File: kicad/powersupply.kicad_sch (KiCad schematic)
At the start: 41 parts, among them Q1 BC547, Q2 BC557, Q3 AO3401A, Q4 AO3401A, SW1 SW_Push, U1 MCP602, U2 INA219AxDCN, U3 STM32F103CBTx, U4 CR2013-MI2120, U5 MCP602, U6 MCP602, U7 MCP602, U8 PCF8574, U9 MCP4725

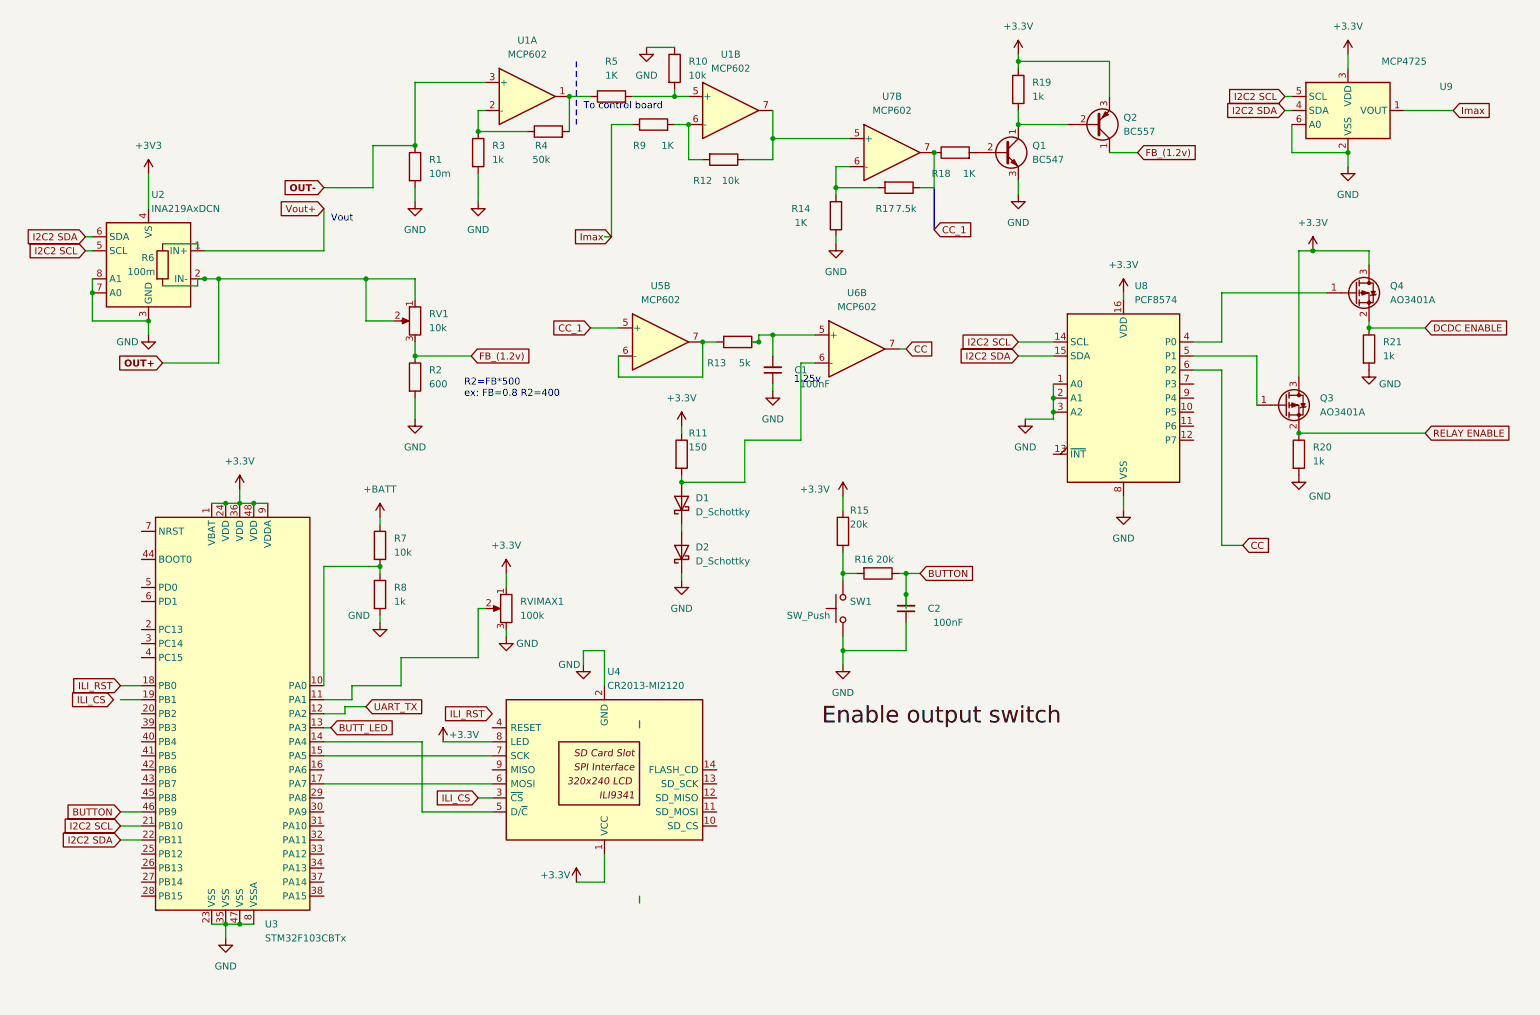
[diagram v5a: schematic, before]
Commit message: update kicad schematic with latched button
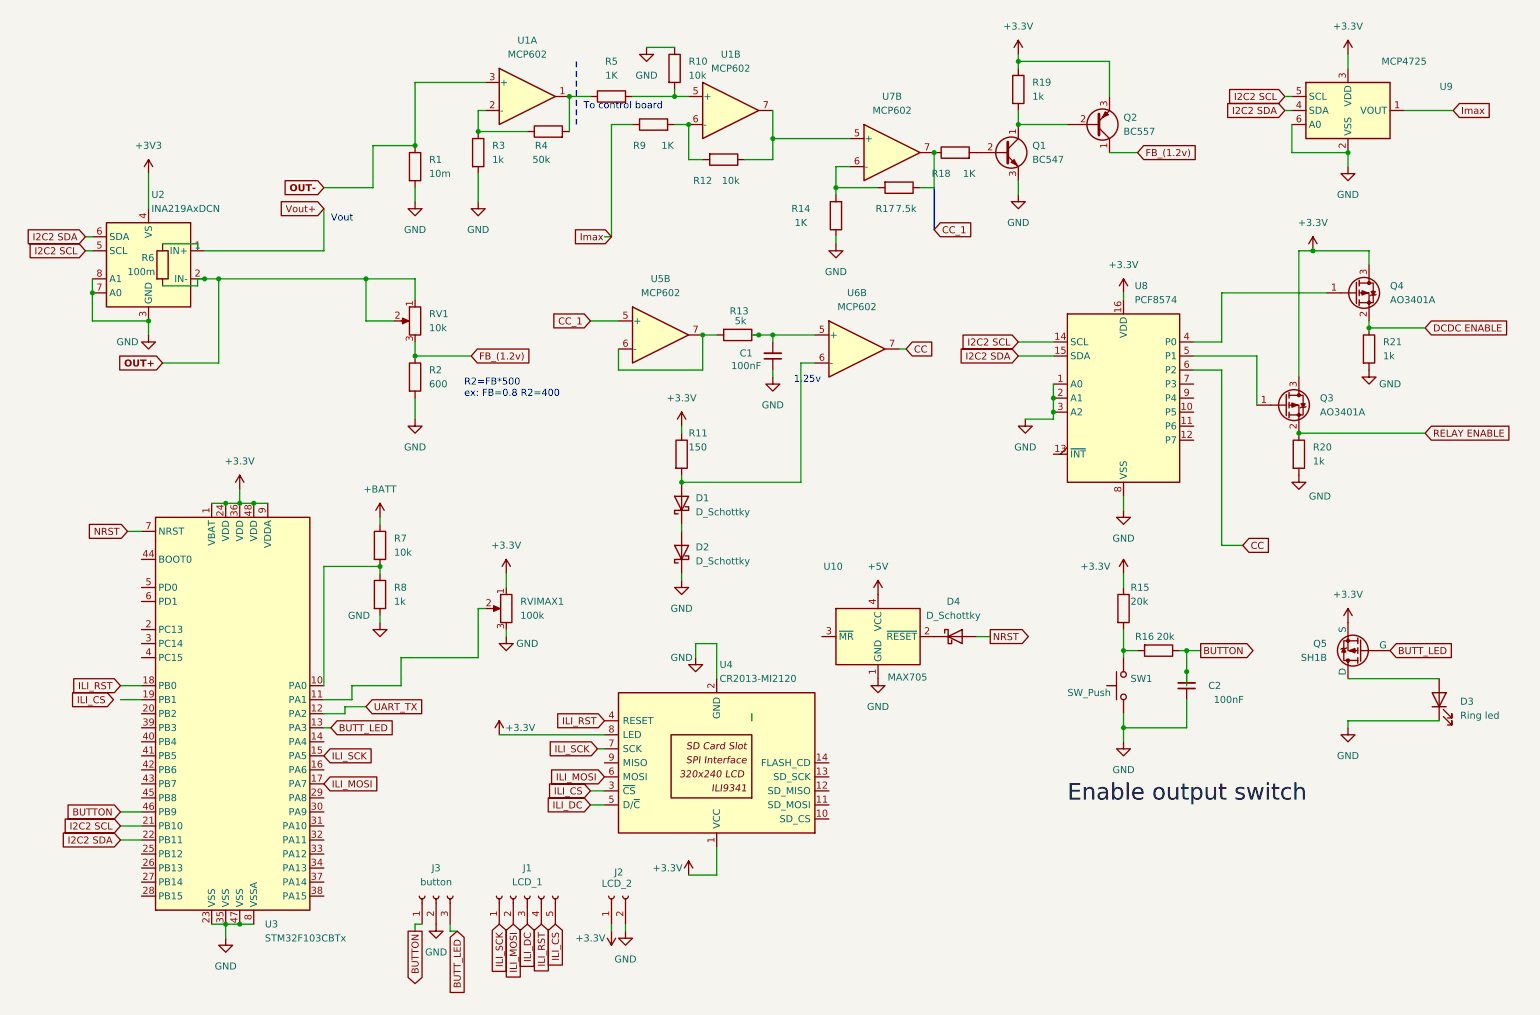
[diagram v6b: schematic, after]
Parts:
- added D3: Ring led, symbol Device:LED
- added D4: D_Schottky, symbol Device:D_Schottky
- added J1: LCD_1, symbol Connector:Conn_01x05_Socket
- added J2: LCD_2, symbol Connector:Conn_01x02_Socket
- added J3: button, symbol Connector:Conn_01x03_Socket
- added Q5: SH1B, symbol Simulation_SPICE:PMOS
- added U10: MAX705, Package_TO_SOT_SMD:SOT-143, symbol Power_Supervisor:MAX811LEUS-T
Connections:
- net +3.3V: now also J2.1 (Pin_1), Q5.3 (S)
- net BUTTON: now also J3.1 (Pin_1)
- net BUTT_LED: now also J3.3 (Pin_3), Q5.2 (G)
- net GND: now also D3.1 (K), J2.2 (Pin_2), J3.2 (Pin_2), U10.1 (GND)
- net ILI_CS: now also J1.5 (Pin_5)
- net ILI_RST: now also U4.4 (RESET), J1.4 (Pin_4)
- net at U3.14 (PA4): no longer U4.5 (D/~{C})
- net ILI_SCK: now reaches U3.15 (PA5), U4.7 (SCK)
- net ILI_SCK: now also J1.1 (Pin_1)
- net ILI_MOSI: now reaches U3.17 (PA7), U4.6 (MOSI)
- net ILI_MOSI: now also J1.2 (Pin_2)
- net NRST: now reaches U3.7 (NRST)
- net NRST: now also D4.2 (A)
- new net: D3.2 (A), Q5.1 (D)
- new net: D4.1 (K), U10.2 (~{RESET})
- new net +5V: U10.4 (VCC)
- new net ILI_DC: J1.3 (Pin_3), U4.5 (D/~{C})
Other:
- moved on the sheet: C1, C2, R13, R15, R16, SW1, U4, U5B

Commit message: complete schematic
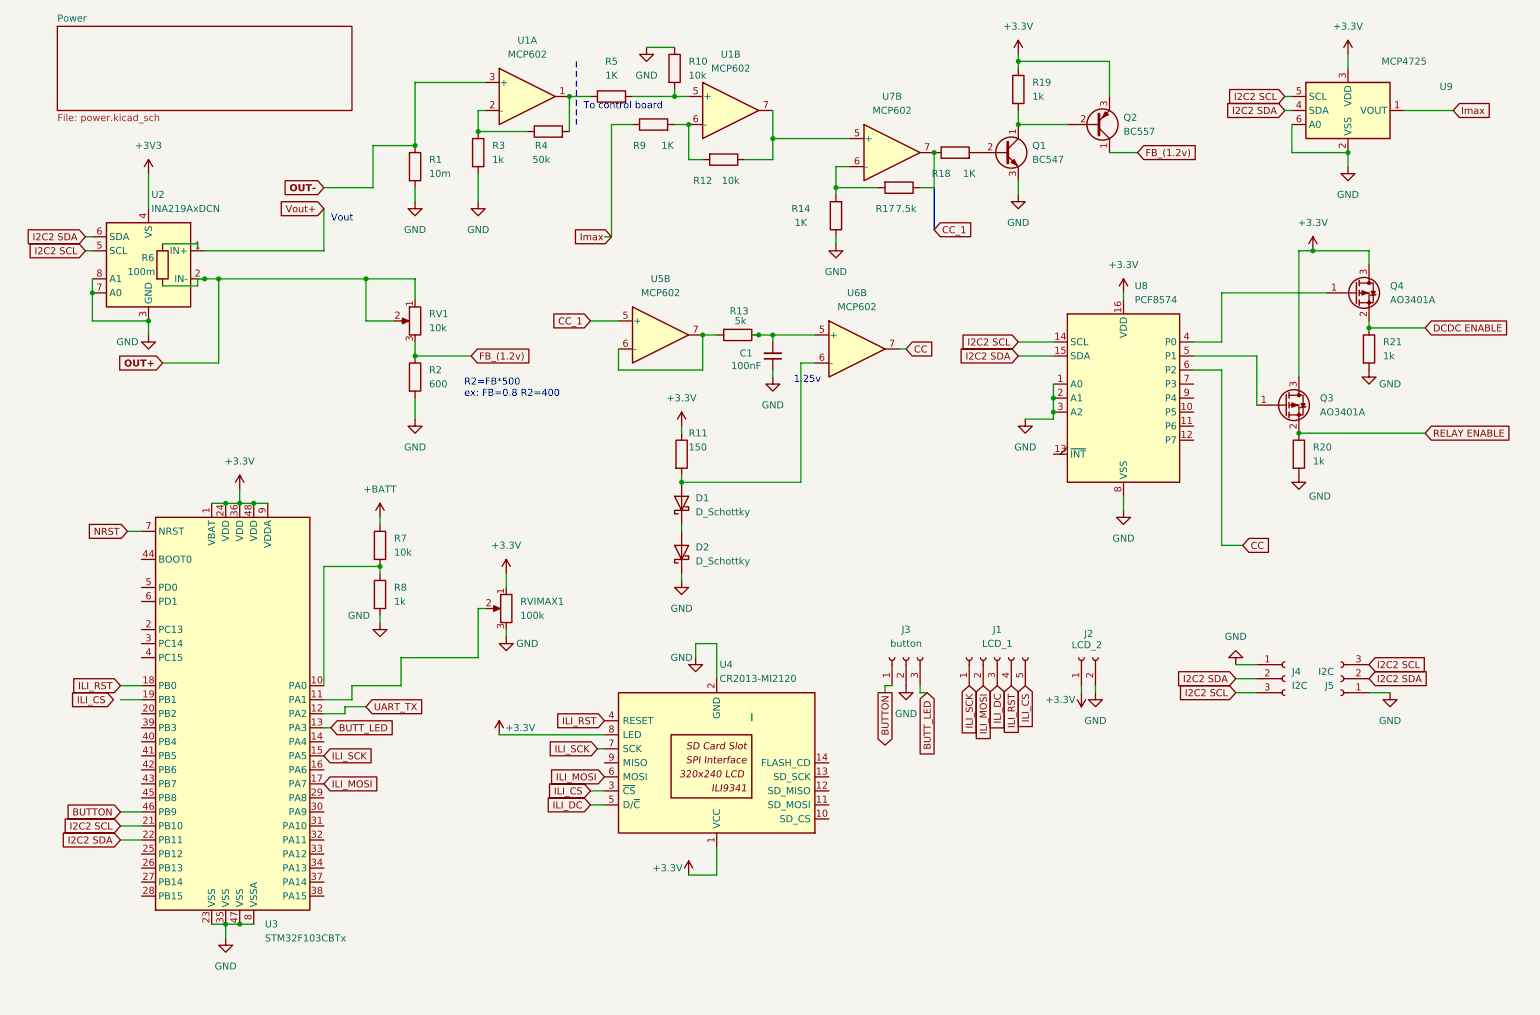
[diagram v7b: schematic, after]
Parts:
- removed C2: 100nF, symbol Device:C_Small
- removed D3: Ring led, symbol Device:LED
- removed D4: D_Schottky, symbol Device:D_Schottky
- removed Q5: SH1B, symbol Simulation_SPICE:PMOS
- removed R15, R16: 20k, Resistor_SMD:R_0603_1608Metric, symbol Device:R
- removed SW1: SW_Push, symbol Switch:SW_Push
- removed U10: MAX705, Package_TO_SOT_SMD:SOT-143, symbol Power_Supervisor:MAX811LEUS-T
- added J4, J5: I2C, symbol Connector:Conn_01x03_Socket
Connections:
- net GND: now also J4.1 (Pin_1), J5.1 (Pin_1)
- net I2C2 SCL: now also J4.3 (Pin_3), J5.3 (Pin_3)
- net I2C2 SDA: now also J4.2 (Pin_2), J5.2 (Pin_2)
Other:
- added sheet Power (power.kicad_sch)
- moved on the sheet: J1, J2, J3
